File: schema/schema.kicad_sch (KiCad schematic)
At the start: 12 parts, among them J1 MCU_ATmega328P_Module, J2 MCU_ATmega328P_Module, J3 LCD_1602_I2C, J5 RF_433MHz_TX, SW1 BTN_MORSE, SW2 BTN_SPEED_UP, SW3 BTN_SPEED_DOWN

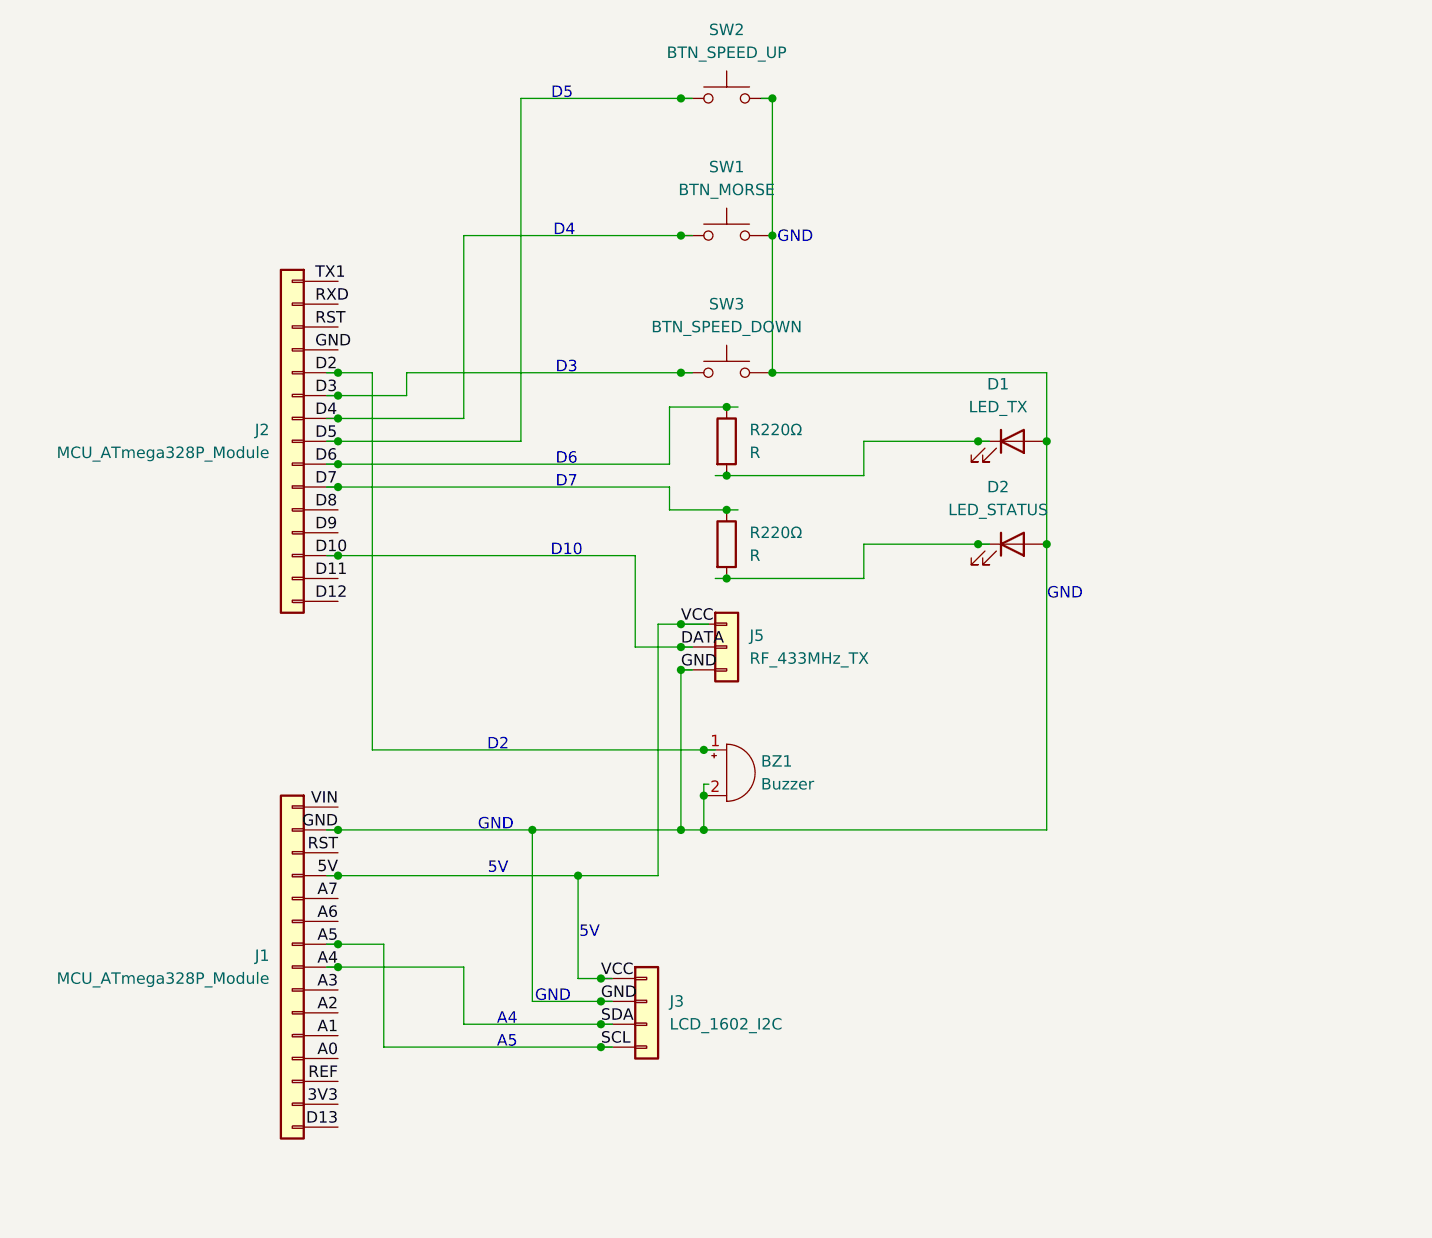
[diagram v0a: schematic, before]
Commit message: Add description to schema
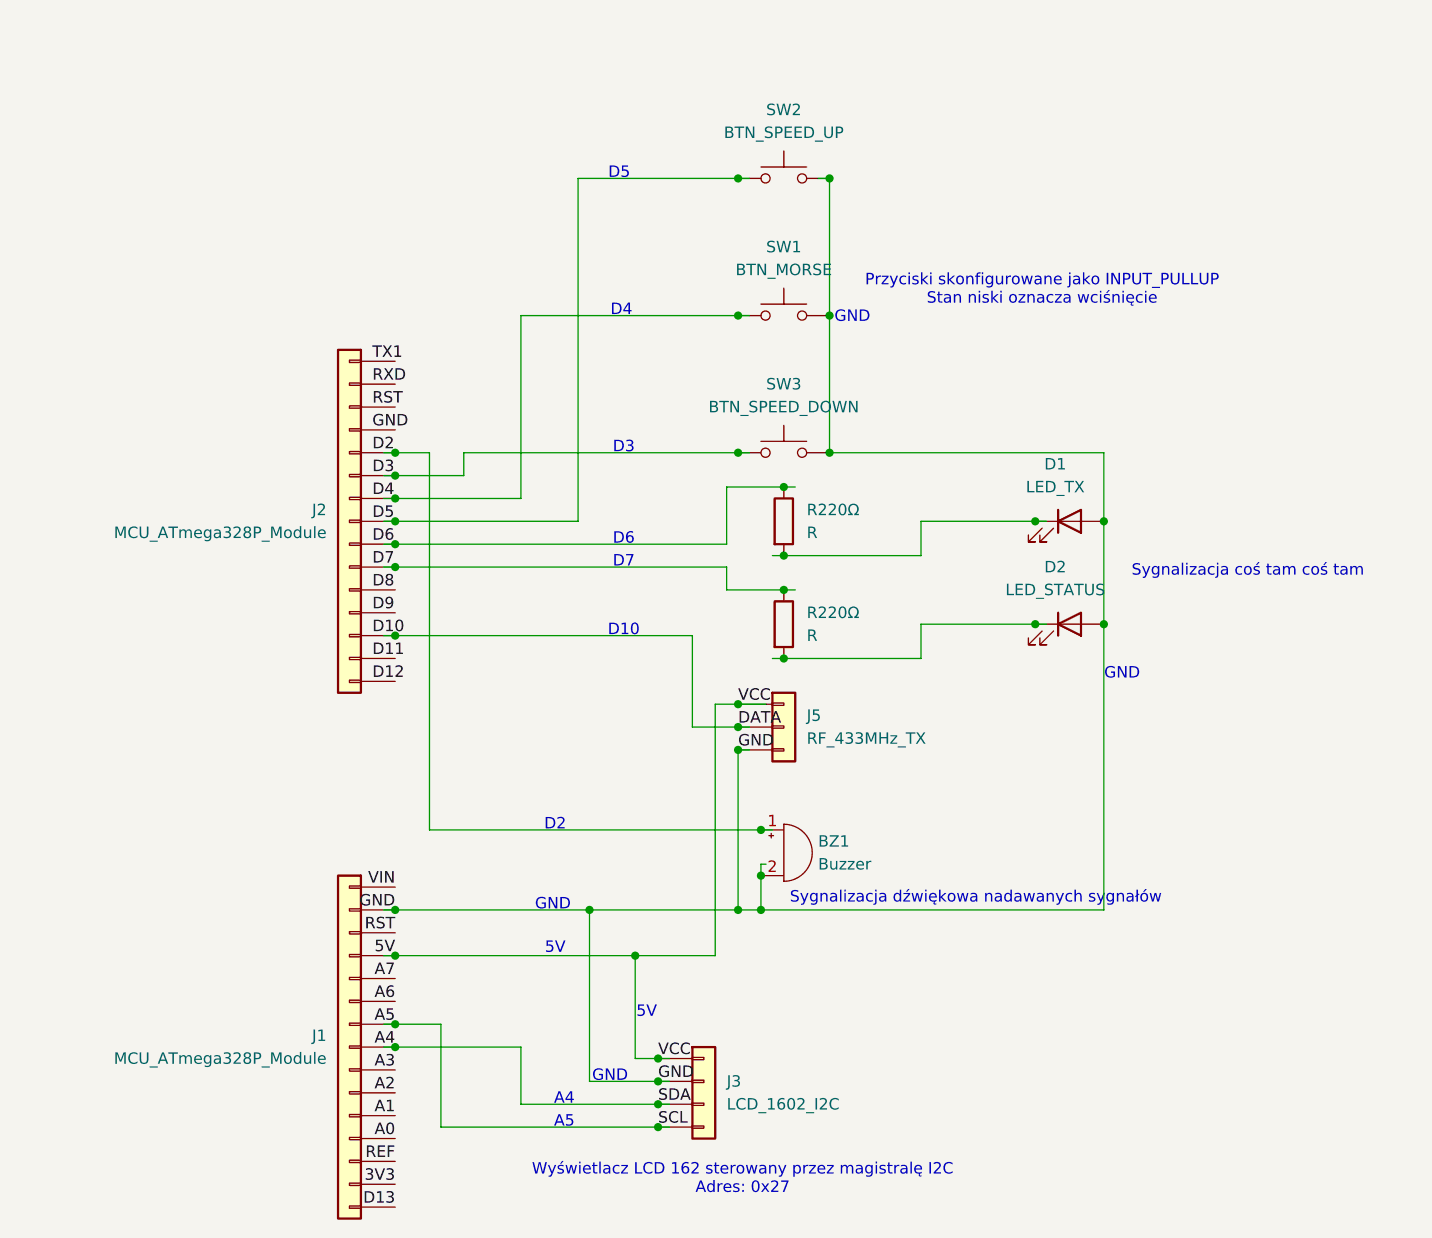
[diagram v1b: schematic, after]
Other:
- note added: "Przyciski skonfigurowane jako INPUT_PULLUP Stan niski oznacza wciśnięcie"
- note added: "Sygnalizacja coś tam coś tam"
- note added: "Sygnalizacja dźwiękowa nadawanych sygnałów"
- note added: "Wyświetlacz LCD 162 sterowany przez magistralę I2C Adres: 0x27"
- moved on the sheet: BZ1, D1, D2, J1, J2, J3, J5, R220Ω, SW1, SW2, SW3
